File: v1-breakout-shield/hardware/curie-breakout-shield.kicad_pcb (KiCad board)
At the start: 2 copper layers, 68.6 x 53.3 mm, 5 parts, among them U1 HOLE, U2 HOLE, U3 HOLE, U4 HOLE, U5 ARDUINO-101-SHIELD

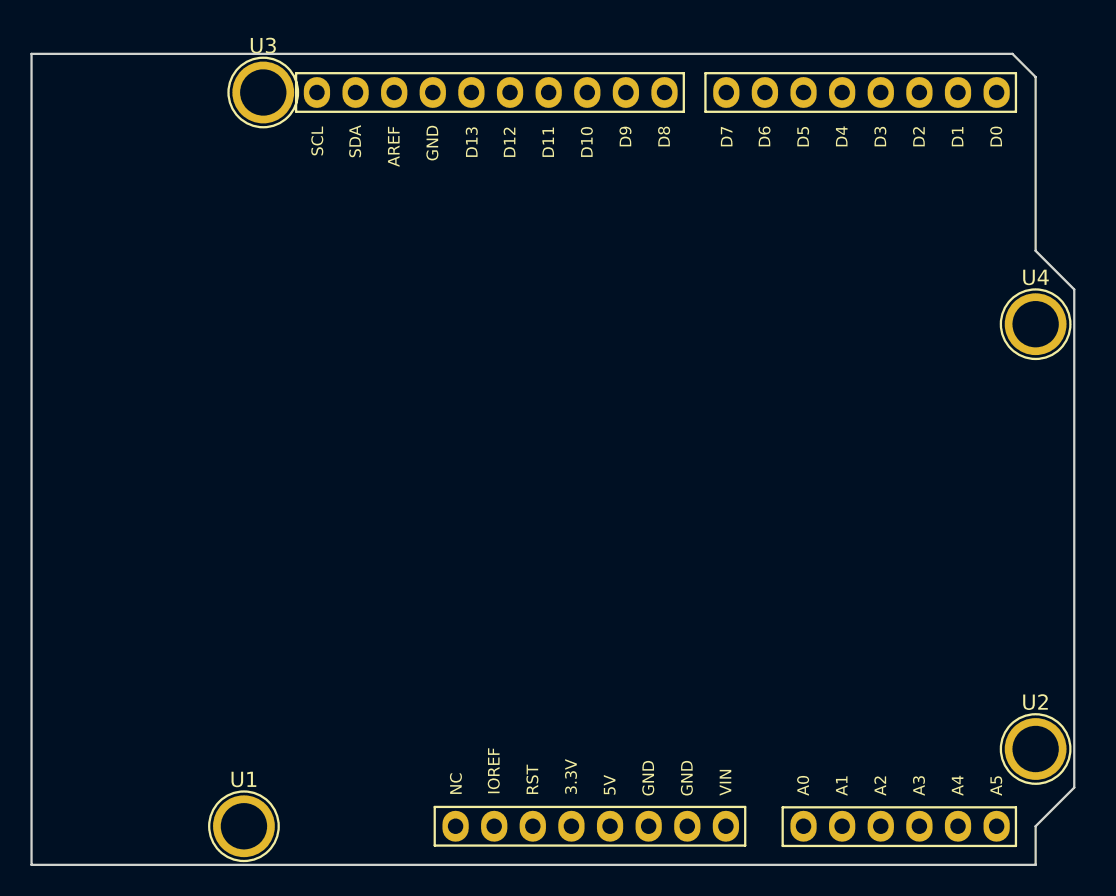
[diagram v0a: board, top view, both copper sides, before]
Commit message: Ordered the breakout board v1.0 from OSH Park.
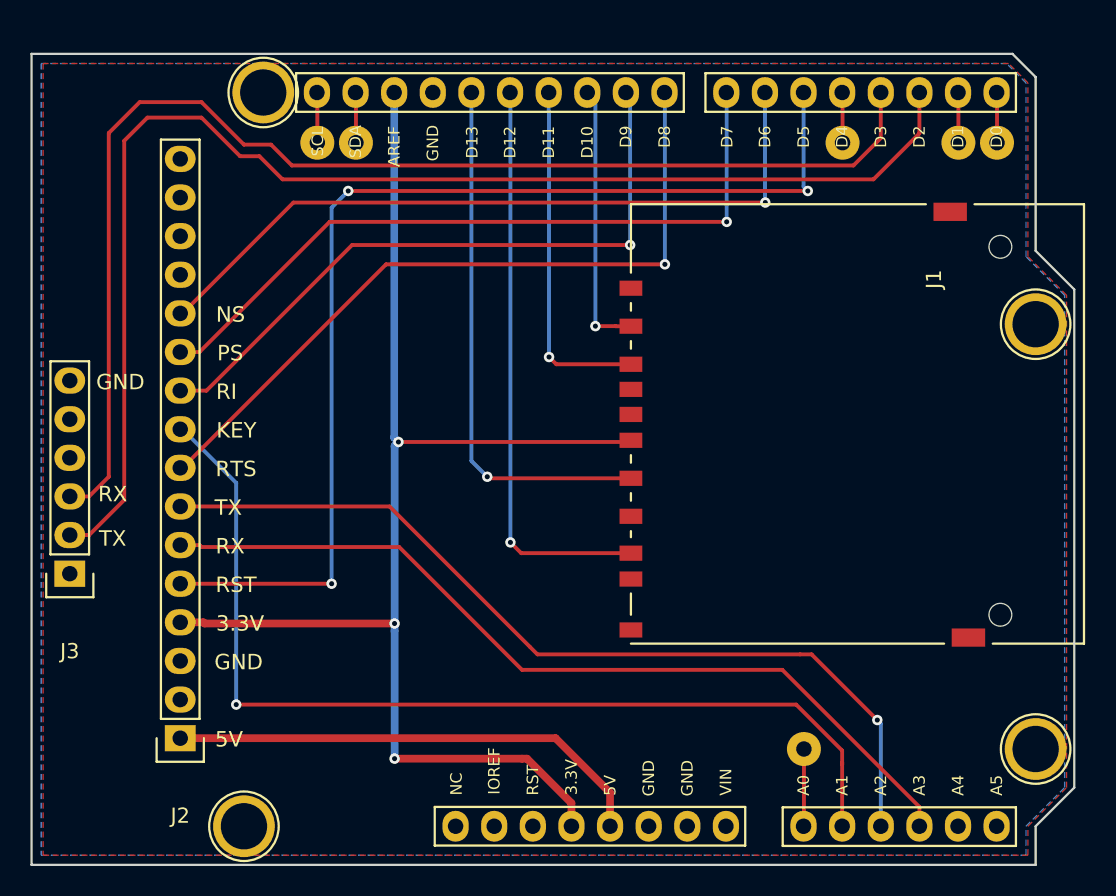
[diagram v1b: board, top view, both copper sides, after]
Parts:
- added J1: CONN-SD-CARD-PUSH-PULL-R/A-SMD, Wickerlib:SD_Holder_FullSize, F.Cu at (150.4, 97.8)
- added J2: FONA808-GPS, Wickerlib:Pin_Header_Straight_1x16, F.Cu at (120.8, 118.0)
- added J3: OBDII-UART, Wickerlib:Pin_Header_Straight_1x06, F.Cu at (113.5, 107.2)
- added W1: D0, Wickerlib:TestHole_1x01, F.Cu at (174.5, 78.9)
- added W2: A0, Wickerlib:TestHole_1x01, F.Cu at (161.8, 118.7)
- added W3: D1, Wickerlib:TestHole_1x01, F.Cu at (172.0, 78.9)
- added W4: A4, Wickerlib:TestHole_1x01, F.Cu at (132.3, 78.9)
- added W5: D4, Wickerlib:TestHole_1x01, F.Cu at (164.3, 78.9)
- added W6: A5, Wickerlib:TestHole_1x01, F.Cu at (129.8, 78.9)
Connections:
- U5 pad 5V: (no net) -> +5V
- U5 pad A0: (no net) -> /A0
- U5 pad A1: (no net) -> /A1(FONA_KEY)
- U5 pad A2: (no net) -> /A2(FONA_TX)
- U5 pad A3: (no net) -> /A3(FONA_RX)
- U5 pad D0: (no net) -> /D0
- U5 pad D1: (no net) -> /D1
- U5 pad D10: (no net) -> /D10(SD_CS)
- U5 pad D11: (no net) -> /D11(MOSI)
- U5 pad D12: (no net) -> /D12(MISO)
- U5 pad D13: (no net) -> /D13(SCLK)
- U5 pad D2: (no net) -> /D2(OBD2_TX)
- U5 pad D3: (no net) -> /D3(OBD2_RX)
- U5 pad D4: (no net) -> /D4
- U5 pad D5: (no net) -> /D5(FONA_RST)
- U5 pad D6: (no net) -> /D6(FONA_NS)
- U5 pad D7: (no net) -> /D7(FONA_PS)
- U5 pad D8: (no net) -> /D8(FONA_RTS)
- U5 pad D9: (no net) -> /D9(FONA_RI)
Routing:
- net +3V3: track 0.00 -> 88.0 mm, vias 0 -> 3
- net /D2(OBD2_TX): track 0.00 -> 86.7 mm
- net /D3(OBD2_RX): track 0.00 -> 82.8 mm
- net /D5(FONA_RST): track 0.00 -> 73.1 mm, vias 0 -> 3
- net /A1(FONA_KEY): track 0.00 -> 66.0 mm, vias 0 -> 1
- net /A2(FONA_TX): track 0.00 -> 58.7 mm, vias 0 -> 1
- net /A3(FONA_RX): track 0.00 -> 57.0 mm
- net /D6(FONA_NS): track 0.00 -> 48.8 mm, vias 0 -> 1
- net /D8(FONA_RTS): track 0.00 -> 48.7 mm, vias 0 -> 1
- net /D7(FONA_PS): track 0.00 -> 48.0 mm, vias 0 -> 1
- net /D9(FONA_RI): track 0.00 -> 43.7 mm, vias 0 -> 1
- net /D12(MISO): track 0.00 -> 37.8 mm, vias 0 -> 1
- net /D13(SCLK): track 0.00 -> 35.2 mm, vias 0 -> 1
- net +5V: track 0.00 -> 32.0 mm
- net /D11(MOSI): track 0.00 -> 23.0 mm, vias 0 -> 1
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- added copper zone on B.Cu, net GND
- added copper zone on F.Cu, net GND
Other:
- board text added: "3.3V"
- board text added: "5V"
- board text added: "Arduino 101 Vehicle Logger Shield v1.0 J1: SD Card 2041021-4 J2: FONA808+GPS Breakout Board J3: OBDII-UART Adapter Board"
- board text added: "GND"
- board text added: "KEY"
- board text added: "NS"
- board text added: "PS"
- board text added: "RI"
- board text added: "RST"
- board text added: "RTS"
- board text added: "RX"
- board text added: "TX"
- board text added: "Wickerbox Electronics 2016"
